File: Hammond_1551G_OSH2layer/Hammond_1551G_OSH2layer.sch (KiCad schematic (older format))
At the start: 2 parts

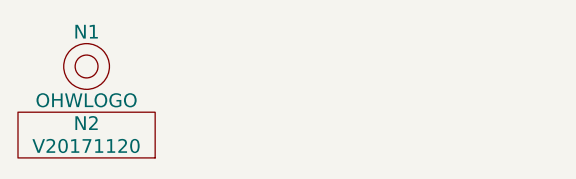
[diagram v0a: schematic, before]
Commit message: DONE: template has Hammond 1551G PCB outline
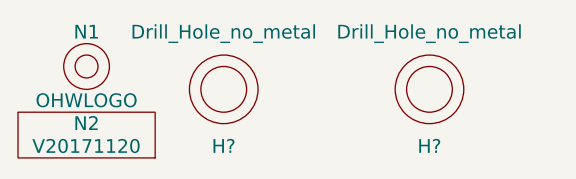
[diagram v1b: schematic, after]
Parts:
- added H? (x2): Drill_Hole_no_metal, SquantorPcbOutline:MountingHole_2.5mm_no_metal, symbol Drill_Hole_no_metal
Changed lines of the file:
@@
 LIBS:SquantorPCBOutline
 LIBS:SquantorProto
+LIBS:Hammond_1551G_OSH2layer-cache
 EELAYER 25 0
 EELAYER END
@@
 	1    0    0    -1
 $EndComp
+$Comp
+L Drill_Hole_no_metal H?
+U 1 1 5B1CFFB9
+P 1450 7450
+F 0 "H?" H 1450 7200 60  0000 C CNN
+F 1 "Drill_Hole_no_metal" H 1450 7700 60  0000 C CNN
+F 2 "SquantorPcbOutline:MountingHole_2.5mm_no_metal" H 1450 7450 60  0001 C CNN
+F 3 "" H 1450 7450 60  0001 C CNN
+	1    1450 7450
+	1    0    0    -1
+$EndComp
+$Comp
+L Drill_Hole_no_metal H?
+U 1 1 5B1D000C
+P 2350 7450
+F 0 "H?" H 2350 7200 60  0000 C CNN
+F 1 "Drill_Hole_no_metal" H 2350 7700 60  0000 C CNN
+F 2 "SquantorPcbOutline:MountingHole_2.5mm_no_metal" H 2350 7450 60  0001 C CNN
+F 3 "" H 2350 7450 60  0001 C CNN
+	1    2350 7450
+	1    0    0    -1
+$EndComp

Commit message: WIP: schematic changes
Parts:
- gave numbers to parts that had none: 2
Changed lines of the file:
@@
 $EndComp
 $Comp
-L Drill_Hole_no_metal H?
+L Drill_Hole_no_metal H1
 U 1 1 5B1CFFB9
 P 1450 7450
-F 0 "H?" H 1450 7200 60  0000 C CNN
+F 0 "H1" H 1450 7200 60  0000 C CNN
 F 1 "Drill_Hole_no_metal" H 1450 7700 60  0000 C CNN
 F 2 "SquantorPcbOutline:MountingHole_2.5mm_no_metal" H 1450 7450 60  0001 C CNN
@@
 $EndComp
 $Comp
-L Drill_Hole_no_metal H?
+L Drill_Hole_no_metal H2
 U 1 1 5B1D000C
 P 2350 7450
-F 0 "H?" H 2350 7200 60  0000 C CNN
+F 0 "H2" H 2350 7200 60  0000 C CNN
 F 1 "Drill_Hole_no_metal" H 2350 7700 60  0000 C CNN
 F 2 "SquantorPcbOutline:MountingHole_2.5mm_no_metal" H 2350 7450 60  0001 C CNN

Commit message: updated hammond 1551G oshpark 2 layer template
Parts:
- H1, H2: symbol Drill_Hole_no_metal -> SquantorPCBOutline:Drill_Hole_no_metal
- N1: symbol OHWLOGO -> SquantorLabels:OHWLOGO
- N2: symbol VYYYYMMDD -> SquantorLabels:VYYYYMMDD
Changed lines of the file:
@@
-EESchema Schematic File Version 2
-LIBS:power
-LIBS:device
-LIBS:switches
-LIBS:relays
-LIBS:motors
-LIBS:transistors
-LIBS:conn
-LIBS:linear
-LIBS:regul
-LIBS:74xx
-LIBS:cmos4000
-LIBS:adc-dac
-LIBS:memory
-LIBS:xilinx
-LIBS:microcontrollers
-LIBS:dsp
-LIBS:microchip
-LIBS:analog_switches
-LIBS:motorola
-LIBS:texas
-LIBS:intel
-LIBS:audio
-LIBS:interface
-LIBS:digital-audio
-LIBS:philips
-LIBS:display
-LIBS:cypress
-LIBS:siliconi
-LIBS:opto
-LIBS:atmel
-LIBS:contrib
-LIBS:valves
-LIBS:SquantorButtons
-LIBS:SquantorConnectors
-LIBS:SquantorLabels
-LIBS:SquantorPCBOutline
-LIBS:SquantorProto
+EESchema Schematic File Version 4
 LIBS:Hammond_1551G_OSH2layer-cache
-EELAYER 25 0
+EELAYER 26 0
 EELAYER END
 $Descr A4 11693 8268
@@
 $EndDescr
 $Comp
-L VYYYYMMDD N2
+L SquantorLabels:VYYYYMMDD N2
 U 1 1 5A1357A5
 P 850 7700
@@
 $EndComp
 $Comp
-L OHWLOGO N1
+L SquantorLabels:OHWLOGO N1
 U 1 1 5A135869
 P 850 7350
@@
 $EndComp
 $Comp
-L Drill_Hole_no_metal H1
+L SquantorPCBOutline:Drill_Hole_no_metal H1
 U 1 1 5B1CFFB9
 P 1450 7450
@@
 $EndComp
 $Comp
-L Drill_Hole_no_metal H2
+L SquantorPCBOutline:Drill_Hole_no_metal H2
 U 1 1 5B1D000C
 P 2350 7450
